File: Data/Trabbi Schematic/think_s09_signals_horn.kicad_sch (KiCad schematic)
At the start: 15 parts, among them J1 Power Outlet (D60), K1 Flasher Relay R3, SW1 Horn Contact (steering wheel), SW2 Turn Signal / Hazard Switch (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, SW3 Driver Door Switch (C30), SW4 Passenger Door Switch (C31), SW5 Tailgate Switch (B10)

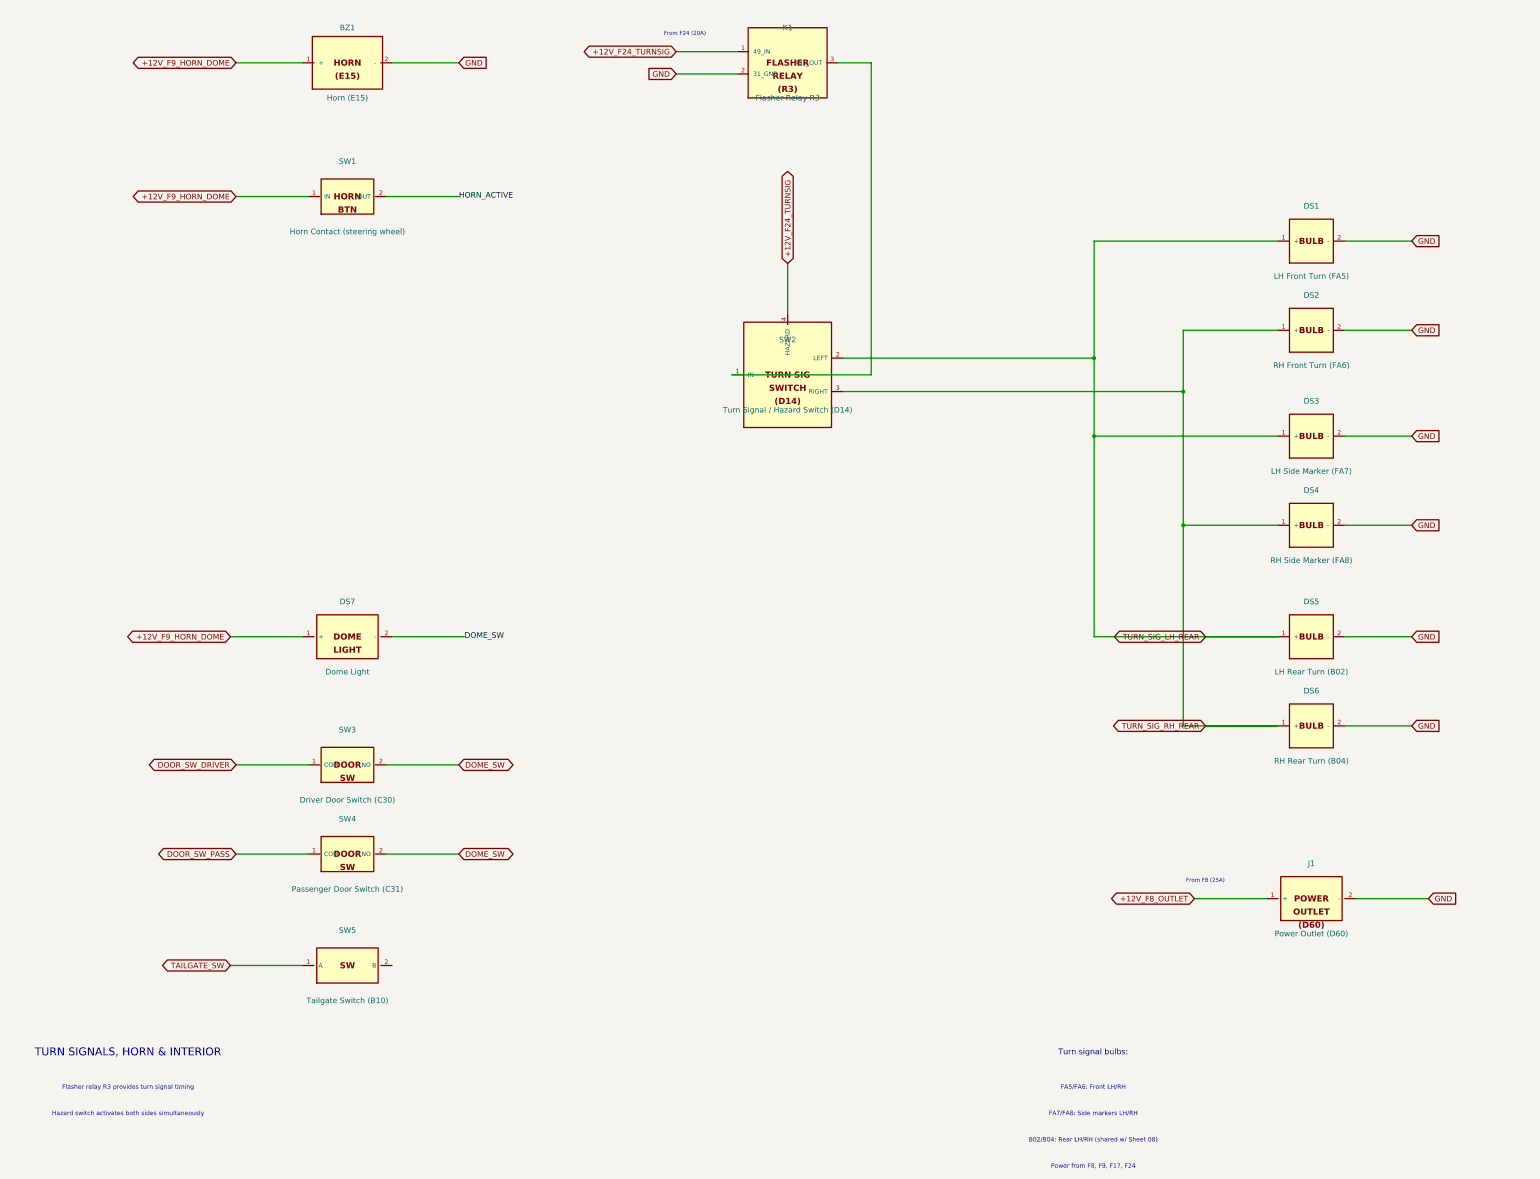
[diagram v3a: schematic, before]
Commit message: Fix label/text positioning: Ref/Value outside body, hide pin numbers
- Reference placed above body edge, Value below (dynamic based on
  symbol height) — no longer overlapping body text
- Pin numbers hidden (clutter, not useful in schematic view)
- Pin name font reduced from 1.016mm to 0.762mm (less overlap)
- Pin length increased from 2.54mm to 3.81mm (more room for pin names
  between body edge and endpoint)
- Store symbol dimensions in _sym_dims for dynamic property placement

Co-Authored-By: Claude Opus 4.6 <noreply@anthropic.com>
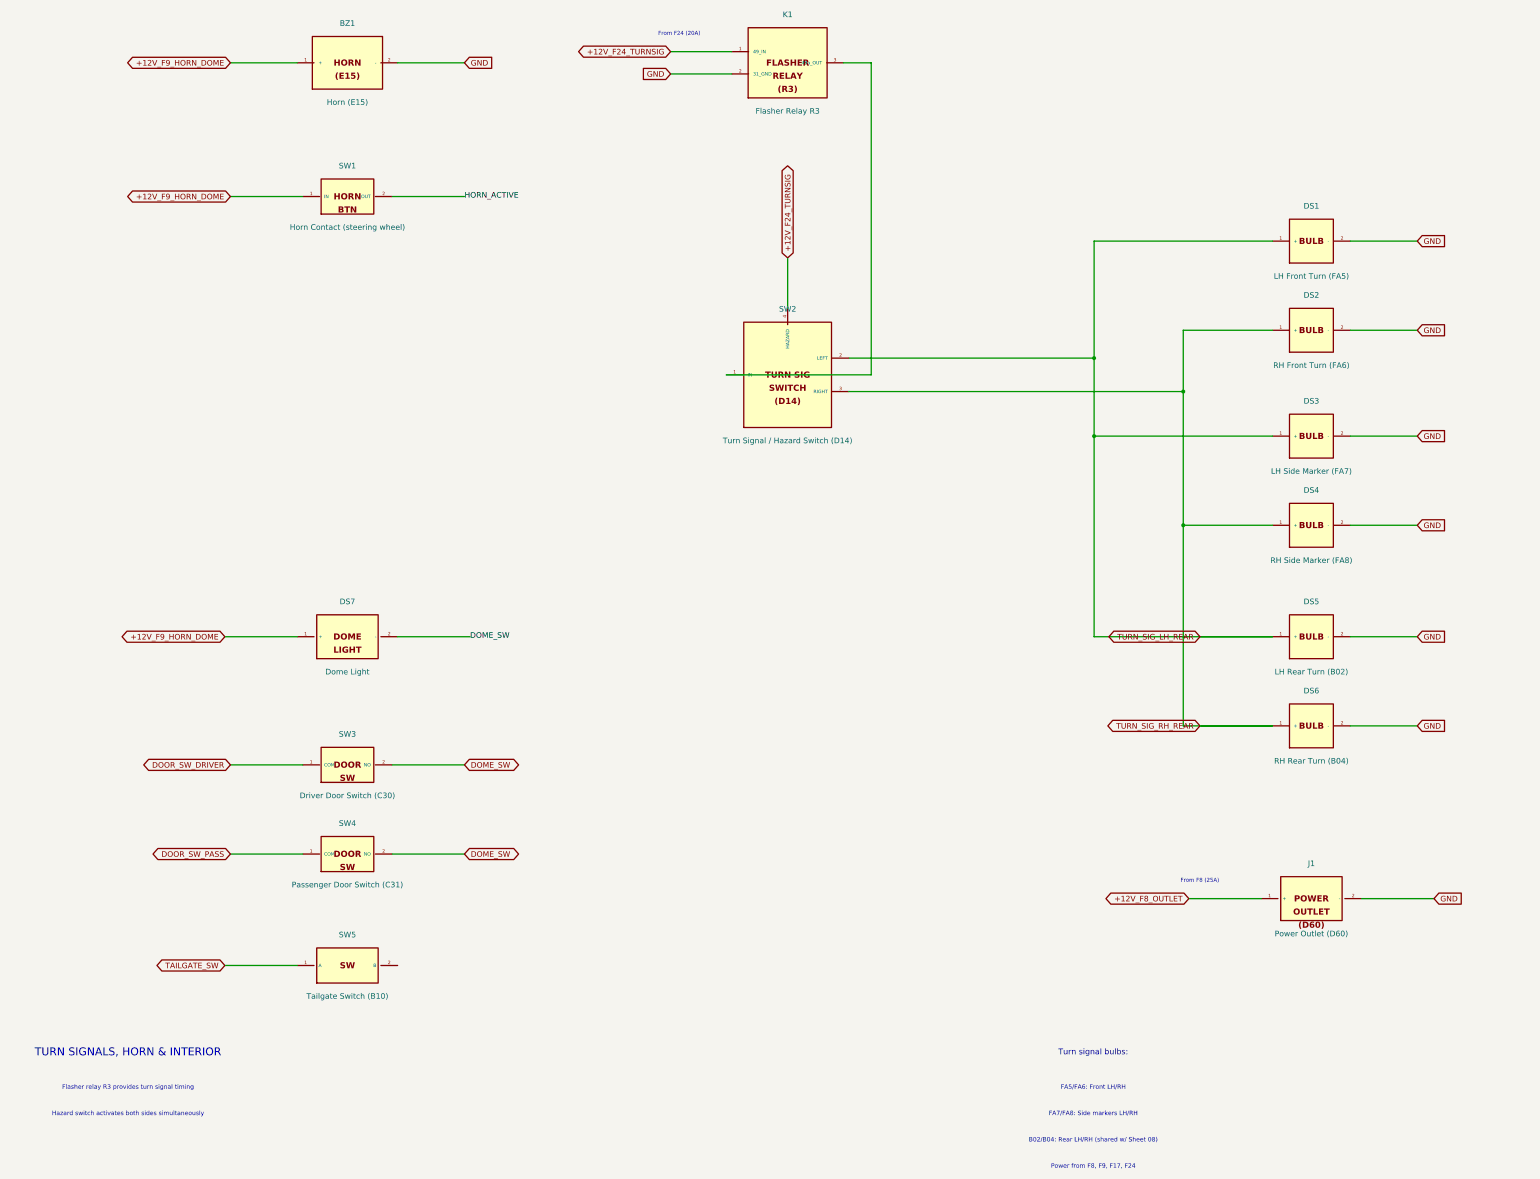
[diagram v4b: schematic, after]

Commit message: Add cross-sheet reference annotations to global labels
- Track all global label positions per sheet during build
- After building all sheets, annotate each global label with
  "→S01,S03,..." text showing which other sheets share the net
- 60 cross-sheet nets identified and annotated
- Two-pass build: 1) build all sheets 2) add cross-refs + save
- Text placed near label in 0.8mm font, offset to avoid overlap

Co-Authored-By: Claude Opus 4.6 <noreply@anthropic.com>
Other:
- note added: "→S01"
- note added: "→S01,S02,S03,S04,S05,S06,S07,S08,S10,S11,S12,S13"
- note added: "→S01,S10,S12"
- note added: "→S08"
- note added: "→S10"
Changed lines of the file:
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@@
     (effects (font (size 1.000 1.000)))
+  )
+  (text "→S01,S10,S12" (at 50.340 41.870 0)
+    (effects (font (size 0.800 0.800)))
+  )
+  (text "→S01,S10,S12" (at 50.340 72.350 0)
+    (effects (font (size 0.800 0.800)))
+  )
+  (text "→S01,S10,S12" (at 49.070 172.680 0)
+    (effects (font (size 0.800 0.800)))
+  )
+  (text "→S01,S02,S03,S04,S05,S06,S07,S08,S10,S11,S12,S13" (at 109.680 41.870 0)
+    (effects (font (size 0.800 0.800)))
+  )
+  (text "→S01,S02,S03,S04,S05,S06,S07,S08,S10,S11,S12,S13" (at 150.670 44.410 0)
+    (effects (font (size 0.800 0.800)))
+  )
+  (text "→S01,S02,S03,S04,S05,S06,S07,S08,S10,S11,S12,S13" (at 326.850 82.510 0)
+    (effects (font (size 0.800 0.800)))
+  )
+  (text "→S01,S02,S03,S04,S05,S06,S07,S08,S10,S11,S12,S13" (at 326.850 102.830 0)
+    (effects (font (size 0.800 0.800)))
+  )
+  (text "→S01,S02,S03,S04,S05,S06,S07,S08,S10,S11,S12,S13" (at 326.850 126.960 0)
+    (effects (font (size 0.800 0.800)))
+  )
+  (text "→S01,S02,S03,S04,S05,S06,S07,S08,S10,S11,S12,S13" (at 326.850 147.280 0)
+    (effects (font (size 0.800 0.800)))
+  )
+  (text "→S01,S02,S03,S04,S05,S06,S07,S08,S10,S11,S12,S13" (at 326.850 172.680 0)
+    (effects (font (size 0.800 0.800)))
+  )
+  (text "→S01,S02,S03,S04,S05,S06,S07,S08,S10,S11,S12,S13" (at 326.850 193.000 0)
+    (effects (font (size 0.800 0.800)))
+  )
+  (text "→S01,S02,S03,S04,S05,S06,S07,S08,S10,S11,S12,S13" (at 330.660 232.370 0)
+    (effects (font (size 0.800 0.800)))
+  )
+  (text "→S01" (at 150.670 39.330 0)
+    (effects (font (size 0.800 0.800)))
+  )
+  (text "→S01" (at 183.340 81.820 0)
+    (effects (font (size 0.800 0.800)))
+  )
+  (text "→S08" (at 271.320 172.680 0)
+    (effects (font (size 0.800 0.800)))
+  )
+  (text "→S08" (at 271.320 193.000 0)
+    (effects (font (size 0.800 0.800)))
+  )
+  (text "→S10" (at 50.340 201.890 0)
+    (effects (font (size 0.800 0.800)))
+  )
+  (text "→S10" (at 50.340 222.210 0)
+    (effects (font (size 0.800 0.800)))
+  )
+  (text "→S10" (at 49.070 247.610 0)
+    (effects (font (size 0.800 0.800)))
+  )
+  (text "→S01" (at 268.780 232.370 0)
+    (effects (font (size 0.800 0.800)))
   )
   (symbol_instances)

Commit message: Fix label text justification for KiCad 9
Add (justify left) to all label and global_label effects.
KiCad 9 requires explicit text justification — without it,
label text is mispositioned relative to the label shape.

Co-Authored-By: Claude Opus 4.6 <noreply@anthropic.com>
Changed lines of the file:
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@@
   )
   (global_label "+12V_F9_HORN_DOME" (shape bidirectional) (at 53.340 39.370 180)
-    (effects (font (size 1.27 1.27)))
+    (effects (font (size 1.27 1.27)) (justify left))
     (property "Intersheetrefs" "${INTERSHEET_REFS}" (at 53.340 39.370 0)
       (effects (font (size 1.27 1.27)) hide)
@@
   )
   (global_label "GND" (shape input) (at 106.680 39.370 0)
-    (effects (font (size 1.27 1.27)))
+    (effects (font (size 1.27 1.27)) (justify left))
     (property "Intersheetrefs" "${INTERSHEET_REFS}" (at 106.680 39.370 0)
       (effects (font (size 1.27 1.27)) hide)
@@
   )
   (global_label "+12V_F9_HORN_DOME" (shape bidirectional) (at 53.340 69.850 180)
-    (effects (font (size 1.27 1.27)))
+    (effects (font (size 1.27 1.27)) (justify left))
     (property "Intersheetrefs" "${INTERSHEET_REFS}" (at 53.340 69.850 0)
       (effects (font (size 1.27 1.27)) hide)
@@
   )
   (label "HORN_ACTIVE" (at 106.680 69.850 0)
-    (effects (font (size 1.27 1.27)))
+    (effects (font (size 1.27 1.27)) (justify left))
   )
   (wire (pts (xy 167.640 36.830) (xy 153.670 36.830))
@@
   )
   (global_label "+12V_F24_TURNSIG" (shape bidirectional) (at 153.670 36.830 180)
-    (effects (font (size 1.27 1.27)))
+    (effects (font (size 1.27 1.27)) (justify left))
     (property "Intersheetrefs" "${INTERSHEET_REFS}" (at 153.670 36.830 0)
       (effects (font (size 1.27 1.27)) hide)
@@
   )
   (global_label "GND" (shape input) (at 153.670 41.910 180)
-    (effects (font (size 1.27 1.27)))
+    (effects (font (size 1.27 1.27)) (justify left))
     (property "Intersheetrefs" "${INTERSHEET_REFS}" (at 153.670 41.910 0)
       (effects (font (size 1.27 1.27)) hide)
@@
   )
   (global_label "+12V_F24_TURNSIG" (shape bidirectional) (at 180.340 83.820 90)
-    (effects (font (size 1.27 1.27)))
+    (effects (font (size 1.27 1.27)) (justify left))
     (property "Intersheetrefs" "${INTERSHEET_REFS}" (at 180.340 83.820 0)
       (effects (font (size 1.27 1.27)) hide)
@@
   )
   (global_label "GND" (shape input) (at 323.850 80.010 0)
-    (effects (font (size 1.27 1.27)))
+    (effects (font (size 1.27 1.27)) (justify left))
     (property "Intersheetrefs" "${INTERSHEET_REFS}" (at 323.850 80.010 0)
       (effects (font (size 1.27 1.27)) hide)
@@
   )
   (global_label "GND" (shape input) (at 323.850 100.330 0)
-    (effects (font (size 1.27 1.27)))
+    (effects (font (size 1.27 1.27)) (justify left))
     (property "Intersheetrefs" "${INTERSHEET_REFS}" (at 323.850 100.330 0)
       (effects (font (size 1.27 1.27)) hide)
@@
   )
   (global_label "GND" (shape input) (at 323.850 124.460 0)
-    (effects (font (size 1.27 1.27)))
+    (effects (font (size 1.27 1.27)) (justify left))
     (property "Intersheetrefs" "${INTERSHEET_REFS}" (at 323.850 124.460 0)
       (effects (font (size 1.27 1.27)) hide)
@@
   )
   (global_label "GND" (shape input) (at 323.850 144.780 0)
-    (effects (font (size 1.27 1.27)))
+    (effects (font (size 1.27 1.27)) (justify left))
     (property "Intersheetrefs" "${INTERSHEET_REFS}" (at 323.850 144.780 0)
       (effects (font (size 1.27 1.27)) hide)
@@
   )
   (global_label "GND" (shape input) (at 323.850 170.180 0)
-    (effects (font (size 1.27 1.27)))
+    (effects (font (size 1.27 1.27)) (justify left))
     (property "Intersheetrefs" "${INTERSHEET_REFS}" (at 323.850 170.180 0)
       (effects (font (size 1.27 1.27)) hide)
@@
   )
   (global_label "GND" (shape input) (at 323.850 190.500 0)
-    (effects (font (size 1.27 1.27)))
+    (effects (font (size 1.27 1.27)) (justify left))
     (property "Intersheetrefs" "${INTERSHEET_REFS}" (at 323.850 190.500 0)
       (effects (font (size 1.27 1.27)) hide)
@@
   )
   (global_label "TURN_SIG_LH_REAR" (shape bidirectional) (at 274.320 170.180 180)
-    (effects (font (size 1.27 1.27)))
+    (effects (font (size 1.27 1.27)) (justify left))
     (property "Intersheetrefs" "${INTERSHEET_REFS}" (at 274.320 170.180 0)
       (effects (font (size 1.27 1.27)) hide)
@@
   )
   (global_label "TURN_SIG_RH_REAR" (shape bidirectional) (at 274.320 190.500 180)
-    (effects (font (size 1.27 1.27)))
+    (effects (font (size 1.27 1.27)) (justify left))
     (property "Intersheetrefs" "${INTERSHEET_REFS}" (at 274.320 190.500 0)
       (effects (font (size 1.27 1.27)) hide)
@@
   )
   (global_label "+12V_F9_HORN_DOME" (shape bidirectional) (at 52.070 170.180 180)
-    (effects (font (size 1.27 1.27)))
+    (effects (font (size 1.27 1.27)) (justify left))
     (property "Intersheetrefs" "${INTERSHEET_REFS}" (at 52.070 170.180 0)
       (effects (font (size 1.27 1.27)) hide)
@@
   )
   (label "DOME_SW" (at 107.950 170.180 0)
-    (effects (font (size 1.27 1.27)))
+    (effects (font (size 1.27 1.27)) (justify left))
   )
   (wire (pts (xy 69.850 199.390) (xy 53.340 199.390))
@@
   )
   (global_label "DOOR_SW_DRIVER" (shape bidirectional) (at 53.340 199.390 180)
-    (effects (font (size 1.27 1.27)))
+    (effects (font (size 1.27 1.27)) (justify left))
     (property "Intersheetrefs" "${INTERSHEET_REFS}" (at 53.340 199.390 0)
       (effects (font (size 1.27 1.27)) hide)
@@
   )
   (global_label "DOME_SW" (shape bidirectional) (at 106.680 199.390 0)
-    (effects (font (size 1.27 1.27)))
+    (effects (font (size 1.27 1.27)) (justify left))
     (property "Intersheetrefs" "${INTERSHEET_REFS}" (at 106.680 199.390 0)
       (effects (font (size 1.27 1.27)) hide)
@@
   )
   (global_label "DOOR_SW_PASS" (shape bidirectional) (at 53.340 219.710 180)
-    (effects (font (size 1.27 1.27)))
+    (effects (font (size 1.27 1.27)) (justify left))
     (property "Intersheetrefs" "${INTERSHEET_REFS}" (at 53.340 219.710 0)
       (effects (font (size 1.27 1.27)) hide)
@@
   )
   (global_label "DOME_SW" (shape bidirectional) (at 106.680 219.710 0)
-    (effects (font (size 1.27 1.27)))
+    (effects (font (size 1.27 1.27)) (justify left))
     (property "Intersheetrefs" "${INTERSHEET_REFS}" (at 106.680 219.710 0)
       (effects (font (size 1.27 1.27)) hide)
@@
   )
   (global_label "TAILGATE_SW" (shape bidirectional) (at 52.070 245.110 180)
-    (effects (font (size 1.27 1.27)))
+    (effects (font (size 1.27 1.27)) (justify left))
     (property "Intersheetrefs" "${INTERSHEET_REFS}" (at 52.070 245.110 0)
       (effects (font (size 1.27 1.27)) hide)
@@
   )
   (global_label "+12V_F8_OUTLET" (shape bidirectional) (at 271.780 229.870 180)
-    (effects (font (size 1.27 1.27)))
+    (effects (font (size 1.27 1.27)) (justify left))
     (property "Intersheetrefs" "${INTERSHEET_REFS}" (at 271.780 229.870 0)
       (effects (font (size 1.27 1.27)) hide)
@@
   )
   (global_label "GND" (shape input) (at 327.660 229.870 0)
-    (effects (font (size 1.27 1.27)))
+    (effects (font (size 1.27 1.27)) (justify left))
     (property "Intersheetrefs" "${INTERSHEET_REFS}" (at 327.660 229.870 0)
       (effects (font (size 1.27 1.27)) hide)
